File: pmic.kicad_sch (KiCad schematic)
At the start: 27 parts, among them U2 MC32PF1510A6EP

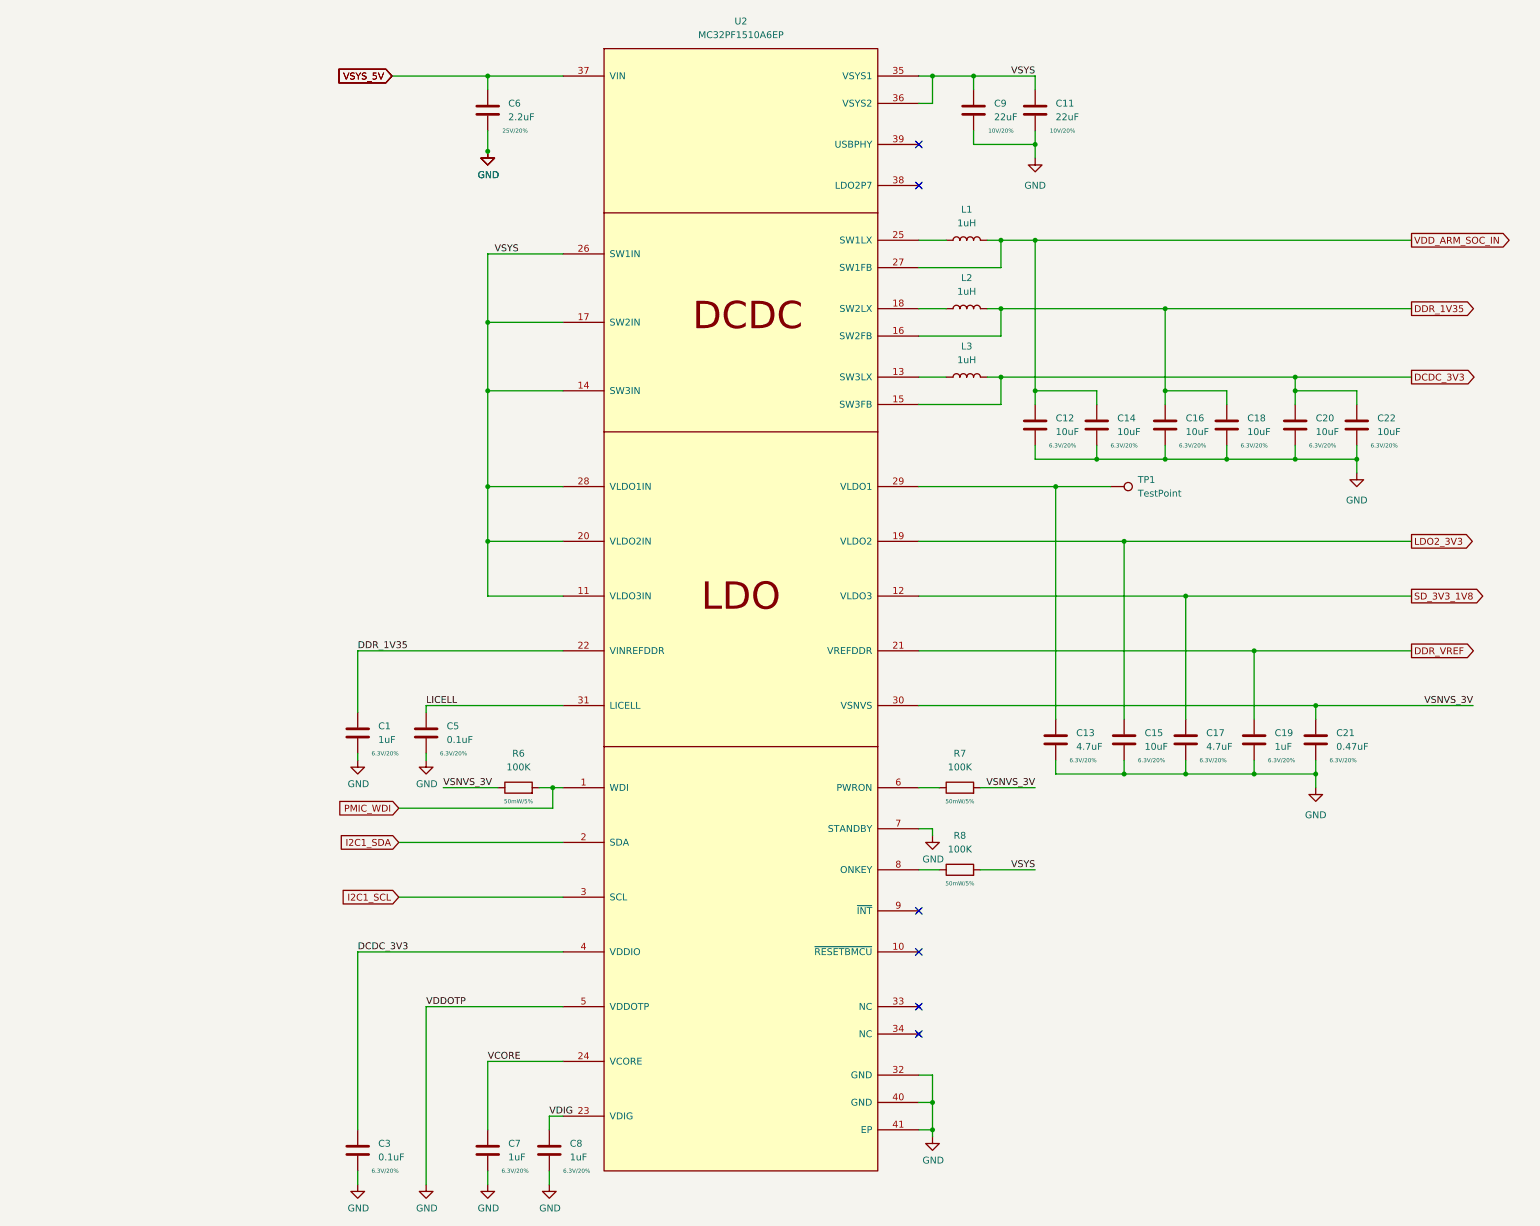
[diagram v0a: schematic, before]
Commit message: more ddr routing, add more connectors
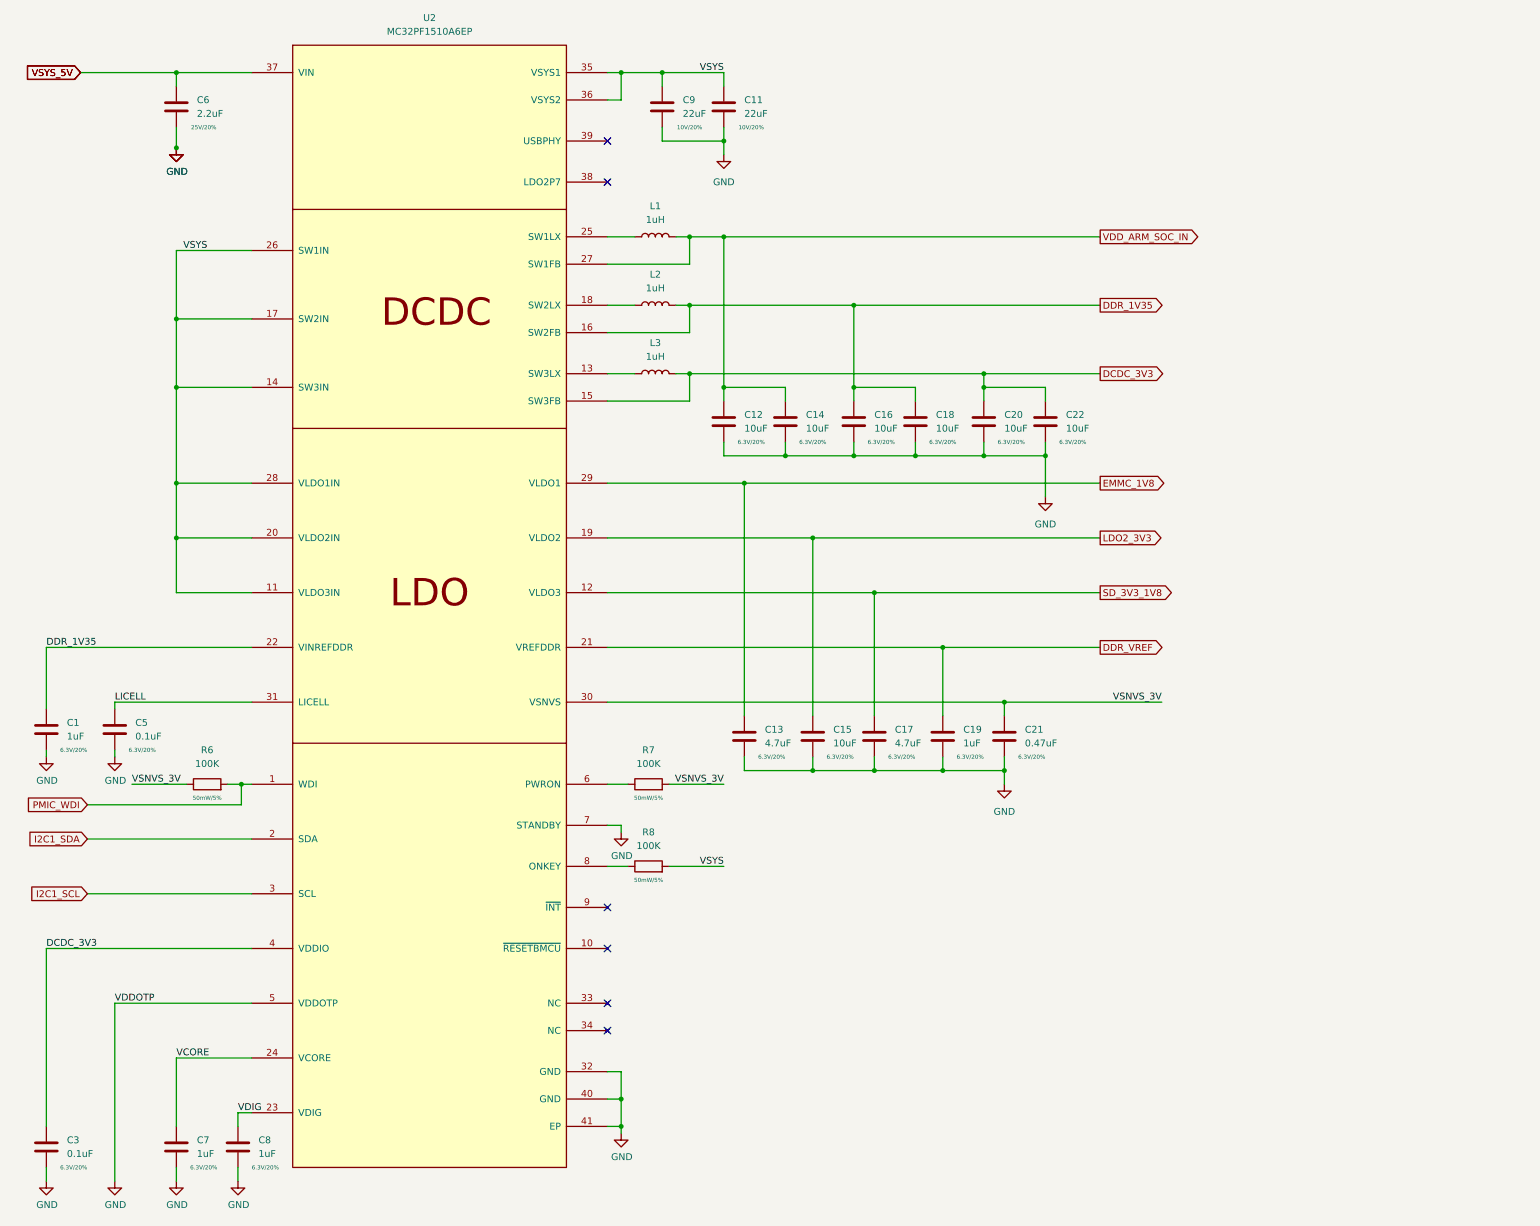
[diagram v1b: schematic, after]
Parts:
- removed TP1: TestPoint, TestPoint:TestPoint_Pad_D1.0mm, symbol Connector:TestPoint
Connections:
- net EMMC_1V8: now reaches C13.1, U2.29 (VLDO1)
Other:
- moved on the sheet: C1, C11, C12, C13, C14, C15, C16, C17, C18, C19, C20, C21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

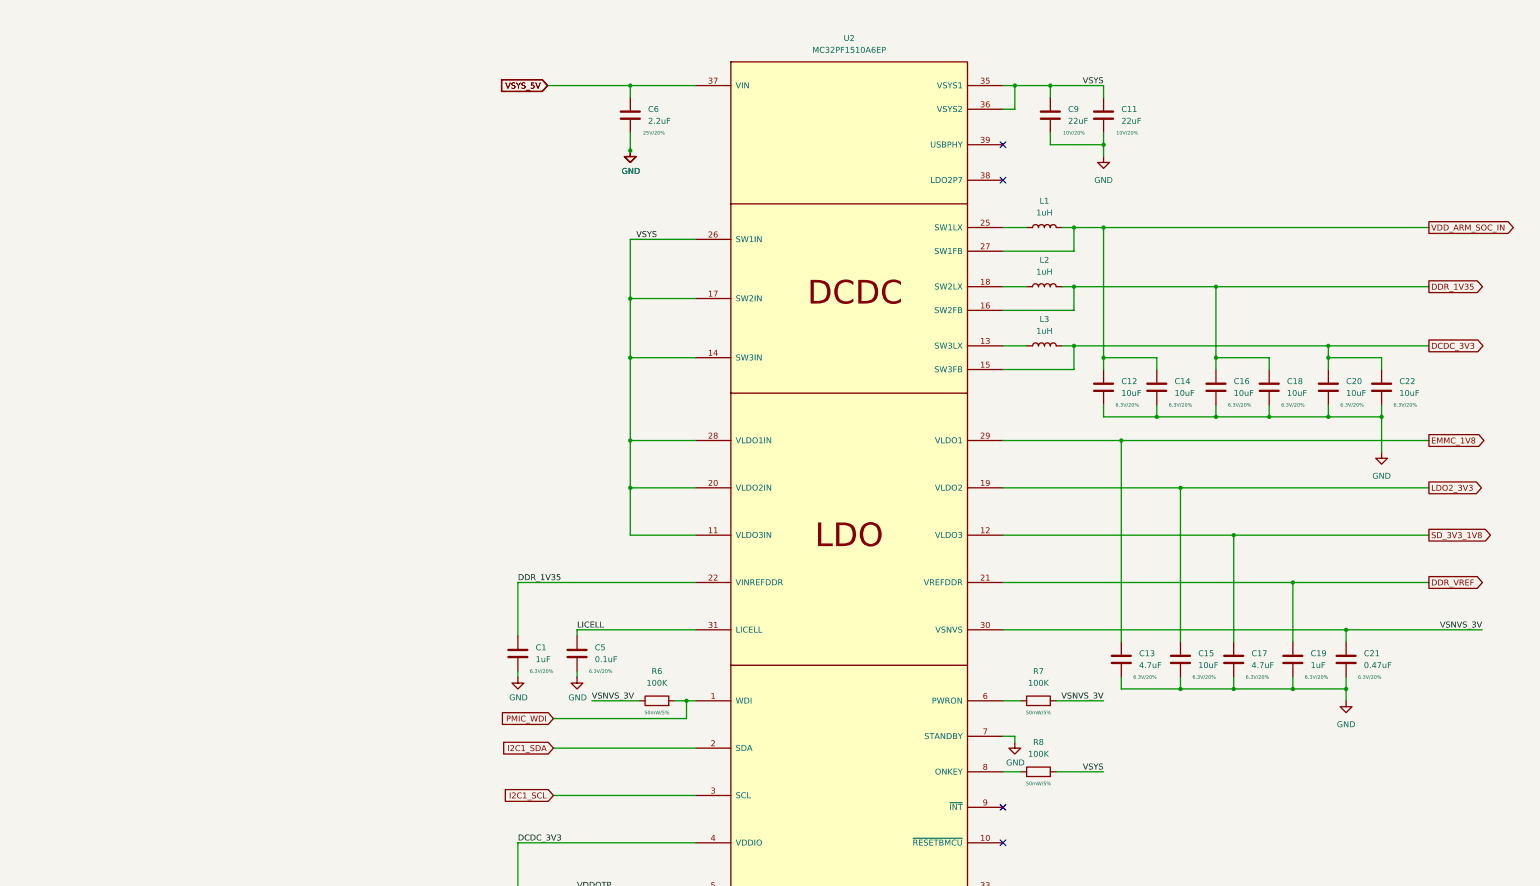
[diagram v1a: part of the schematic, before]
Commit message: start moving to hierarchal labels, add emmc
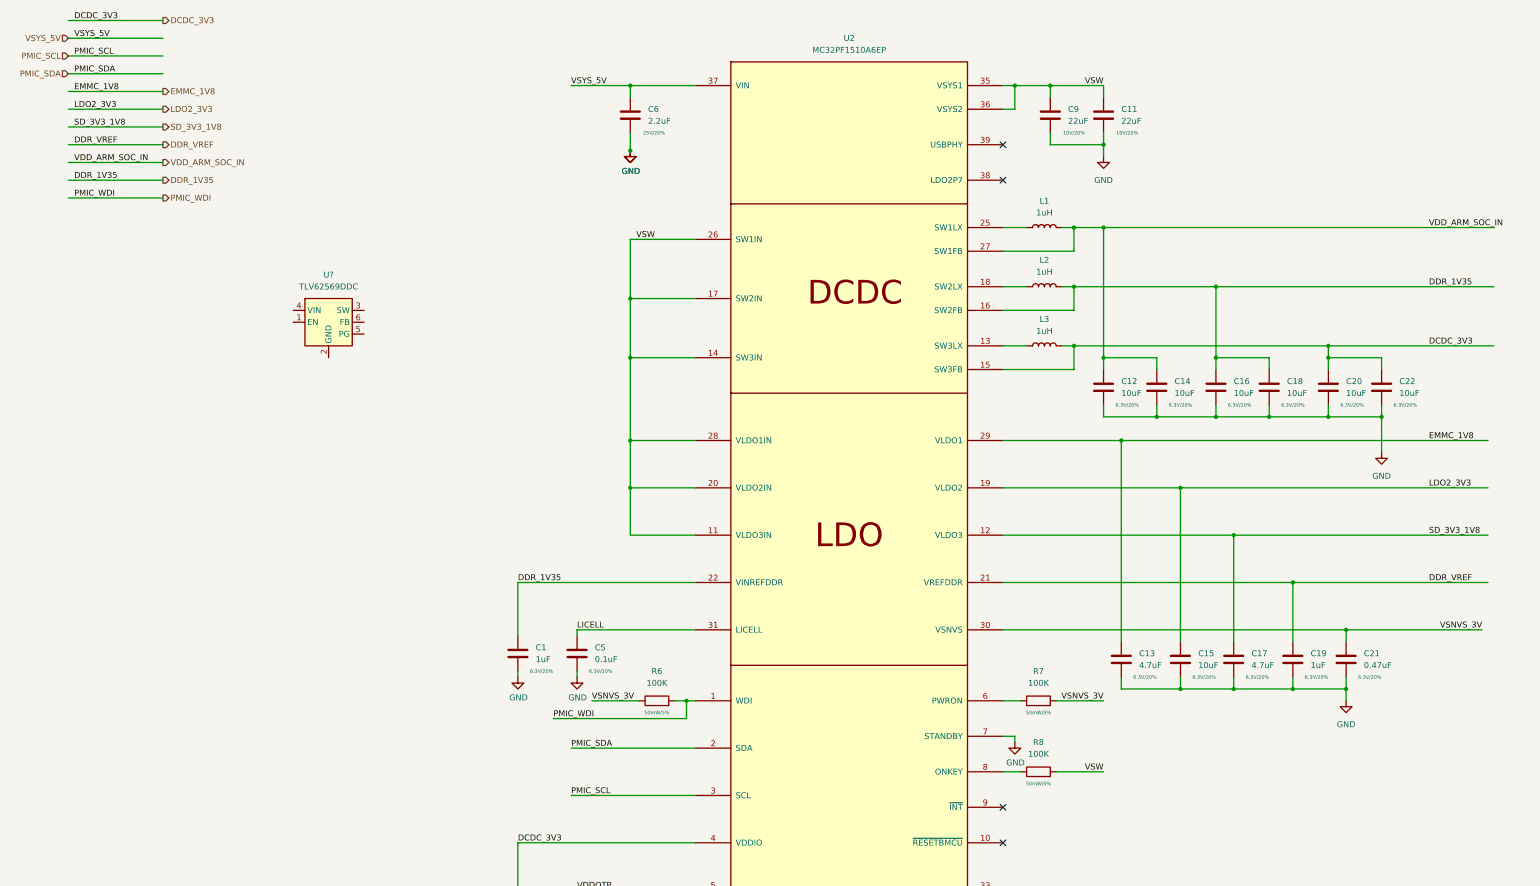
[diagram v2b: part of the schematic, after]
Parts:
- added U?: TLV62569DDC, Package_TO_SOT_SMD:SOT-23-6, symbol Regulator_Switching:TLV62569DDC
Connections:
- net I2C1_SCL renamed PMIC_SCL
- net I2C1_SDA renamed PMIC_SDA
- net VSYS renamed VSW
